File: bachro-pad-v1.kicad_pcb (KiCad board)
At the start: 2 copper layers, 12 x 20.6 mm, 39 parts, among them J0 OLED_128x32, SW1 RotaryEncoder_Switch, SW10 RotaryEncoder_Switch, SW11 RotaryEncoder_Switch, SW12 RotaryEncoder_Switch, SW13 RotaryEncoder_Switch, SW14 RotaryEncoder_Switch, SW15 RotaryEncoder_Switch, SW16 RotaryEncoder_Switch, SW2 RotaryEncoder_Switch, SW3 RotaryEncoder_Switch, SW4 RotaryEncoder_Switch, SW5 RotaryEncoder_Switch, SW6 RotaryEncoder_Switch, SW7 RotaryEncoder_Switch, SW8 RotaryEncoder_Switch, SW9 RotaryEncoder_Switch, U1 rp2040-zero, U2 MCP23017x-x-SP, U3 MCP23017x-x-SP, U4 TRRS

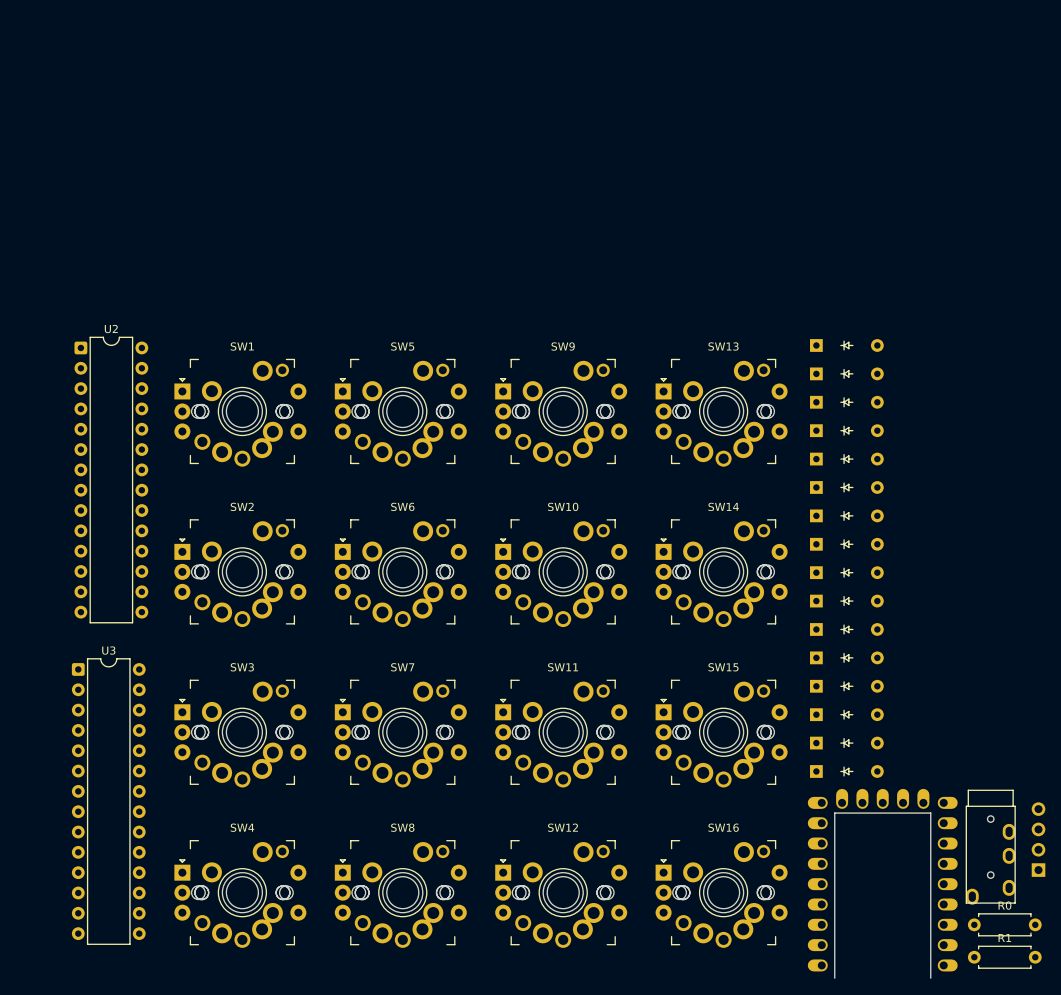
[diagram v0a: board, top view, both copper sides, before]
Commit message: Sync PCB with schematic: add decoupling caps and INT pull-up footprints
Update PCB from Schematic after adding C0/C1 (MCP23017 decoupling) and
R3-R6 (INTA/INTB pull-ups) in the schematic.
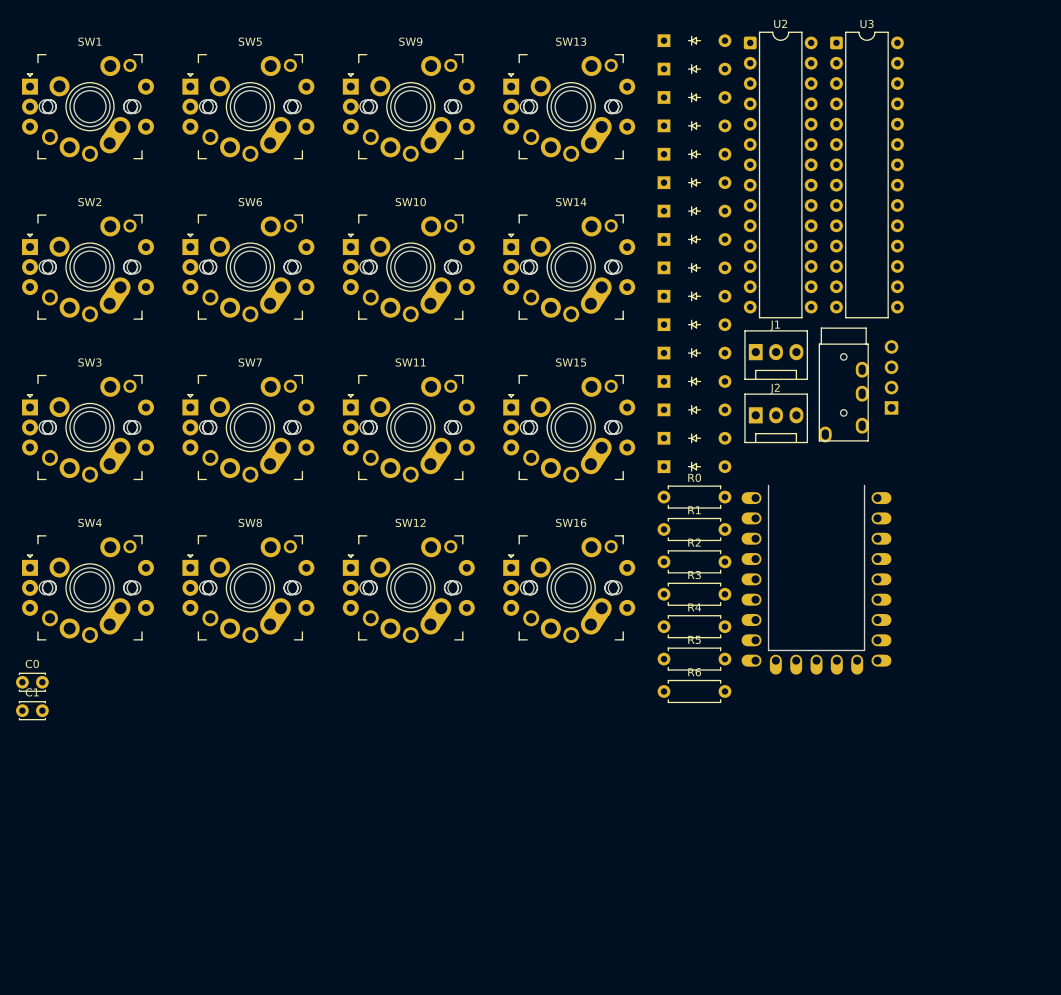
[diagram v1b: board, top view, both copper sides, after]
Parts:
- added C0: 100nF, Capacitor_THT:C_Disc_D3.0mm_W2.0mm_P2.50mm, F.Cu at (305.9, 81.5)
- added C1: 100nF, Capacitor_THT:C_Disc_D3.0mm_W2.0mm_P2.50mm, F.Cu at (305.9, 85.0)
- added J1: Conn_01x03, Connector:FanPinHeader_1x03_P2.54mm_Vertical, F.Cu at (397.5, 40.2)
- added J2: Conn_01x03, Connector:FanPinHeader_1x03_P2.54mm_Vertical, F.Cu at (397.5, 48.1)
- added R2: 10k, Resistor_THT:R_Axial_DIN0207_L6.3mm_D2.5mm_P7.62mm_Horizontal, F.Cu at (386.1, 66.4)
- added R3: 10k, Resistor_THT:R_Axial_DIN0207_L6.3mm_D2.5mm_P7.62mm_Horizontal, F.Cu at (386.1, 70.5)
- added R4: 10k, Resistor_THT:R_Axial_DIN0207_L6.3mm_D2.5mm_P7.62mm_Horizontal, F.Cu at (386.1, 74.5)
- added R5: 10k, Resistor_THT:R_Axial_DIN0207_L6.3mm_D2.5mm_P7.62mm_Horizontal, F.Cu at (386.1, 78.6)
- added R6: 10k, Resistor_THT:R_Axial_DIN0207_L6.3mm_D2.5mm_P7.62mm_Horizontal, F.Cu at (386.1, 82.6)
- R0, R1: value Resistor -> 4.7k
- moved U3 122.9 mm to (407.6, 1.55)
- moved U2 91.9 mm to (396.9, 1.55)
- moved R0 66.1 mm to (386.1, 58.3)
- moved R1 66.1 mm to (386.1, 62.4)
- moved J0 60.6 mm to (412.9, 37.4)
- moved U4 60.6 mm to (408.5, 39.2)
- moved D1 42.6 mm to (386.1, 1.27)
- moved D10 42.6 mm to (386.1, 33.2)
- moved D11 42.6 mm to (386.1, 36.8)
- moved D14 42.6 mm to (386.1, 47.4)
- moved D15 42.6 mm to (386.1, 51.0)
- moved D16 42.6 mm to (386.1, 54.5)
- moved D3 42.6 mm to (386.1, 8.38)
- moved D5 42.6 mm to (386.1, 15.5)
- moved D6 42.6 mm to (386.1, 19.0)
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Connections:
- J0 pad 2: 3V3 -> +3V3
- U1 pad 17: unconnected-(U1-26-Pad17) -> DEBUG_TX
- U1 pad 18: unconnected-(U1-27-Pad18) -> DEBUG_RX
- U1 pad 19: unconnected-(U1-28-Pad19) -> TETHER_DETECT
- U1 pad 20: unconnected-(U1-29-Pad20) -> SPARE_ADC
- U1 pad 21: 3V3 -> +3V3
- U2 pad 18: 3V3 -> +3V3
- U2 pad 9: 3V3 -> +3V3
- U3 pad 15: 3V3 -> +3V3
- U3 pad 18: 3V3 -> +3V3
- U3 pad 9: 3V3 -> +3V3
- U4 pad 3: 3V3 -> TETHER_DETECT

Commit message: First draft
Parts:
- J1, J2, U1: moved to B.Cu
- moved U3 303.5 mm to (121.3, 102.2), turned to 180 degrees
- moved U1 285.7 mm to (124.0, 17.8), turned to -90 degrees
- moved U2 282.3 mm to (121.4, 63.3), turned to 180 degrees
- moved R0 267.3 mm to (124.0, 6.10)
- moved J0 262.4 mm to (150.8, 24.4), turned to 180 degrees
- moved R1 258.2 mm to (134.1, 6.10)
- moved SW13 255.9 mm to (133.3, 95.2)
- moved R2 242.0 mm to (151.8, 6.10), turned to 180 degrees
- moved R6 236.9 mm to (161.9, 6.10), turned to 180 degrees
- moved SW14 231.6 mm to (152.4, 95.2)
- moved J1 231.2 mm to (168.3, 10.2), turned to -90 degrees
- moved SW9 230.9 mm to (133.3, 76.2)
- moved D1 229.9 mm to (156.8, 19.1), turned to -90 degrees
- moved D5 226.7 mm to (159.4, 19.1), turned to -90 degrees
- moved R5 225.9 mm to (172.1, 6.10), turned to 180 degrees
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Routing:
- net gnd: track 0.00 -> 522.2 mm, vias 0 -> 3
- net +3V3: track 0.00 -> 223.4 mm, vias 0 -> 3
- net col 4: track 0.00 -> 197.1 mm
- net col 3: track 0.00 -> 189.1 mm
- net col 2: track 0.00 -> 184.3 mm
- net col 1: track 0.00 -> 147.9 mm, vias 0 -> 1
- net SDA: track 0.00 -> 124.5 mm, vias 0 -> 1
- net U3 INTA: track 0.00 -> 124.5 mm, vias 0 -> 2
- net SCL: track 0.00 -> 114.6 mm, vias 0 -> 1
- net U3 INTB: track 0.00 -> 111.9 mm, vias 0 -> 2
- net U2 INTA: track 0.00 -> 110.0 mm, vias 0 -> 2
- net Net-(D13-A): track 0.00 -> 106.8 mm
- net Net-(D14-A): track 0.00 -> 98.5 mm
- net row 1: track 0.00 -> 94.9 mm, vias 0 -> 3
- net U2 INTB: track 0.00 -> 93.3 mm, vias 0 -> 2
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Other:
- board size 12 x 20.6 mm -> 89.5 x 103.5 mm
- board text added: "+3v3"
- board text added: "BACHROPAD"
- board text added: "GND"
- board text added: "GP29"
- board text added: "RX"
- board text added: "TX"
- board text added: "by joni"

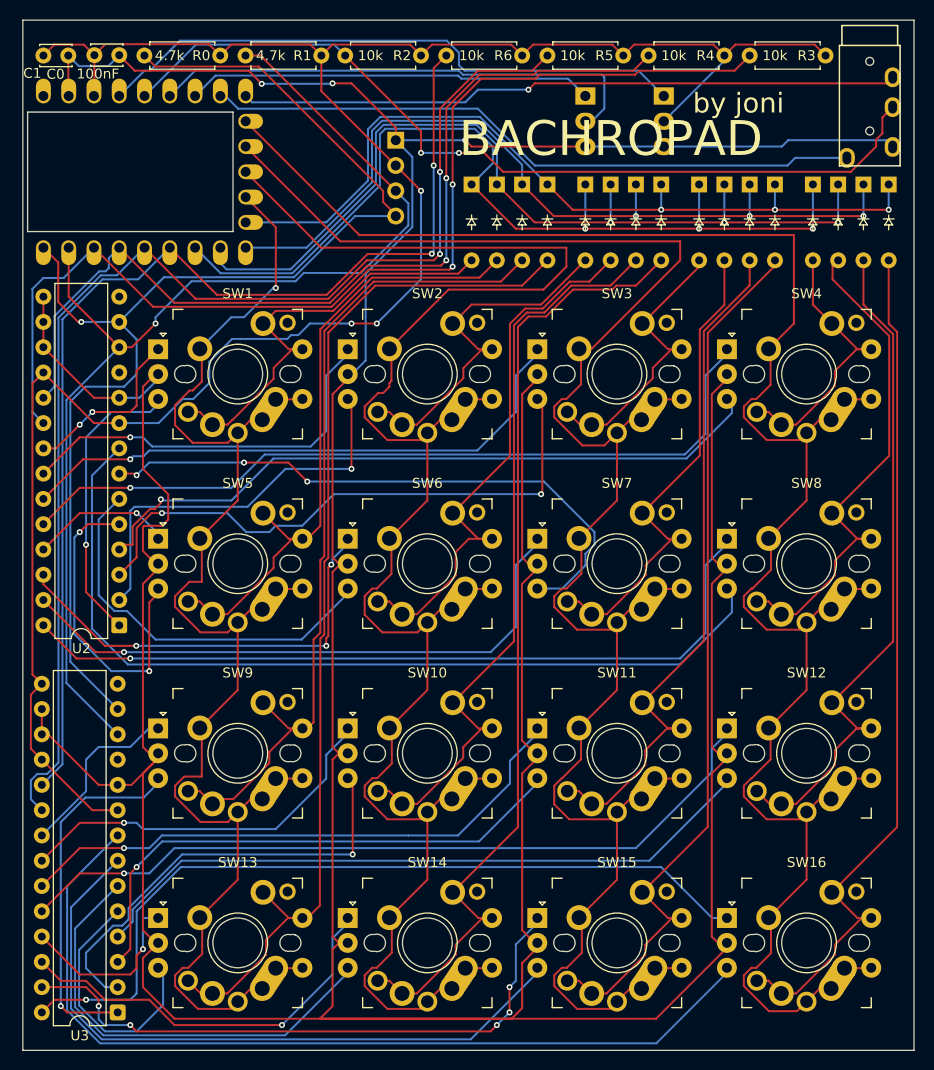
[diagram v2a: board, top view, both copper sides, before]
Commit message: updating layout to fix silk screen warnings
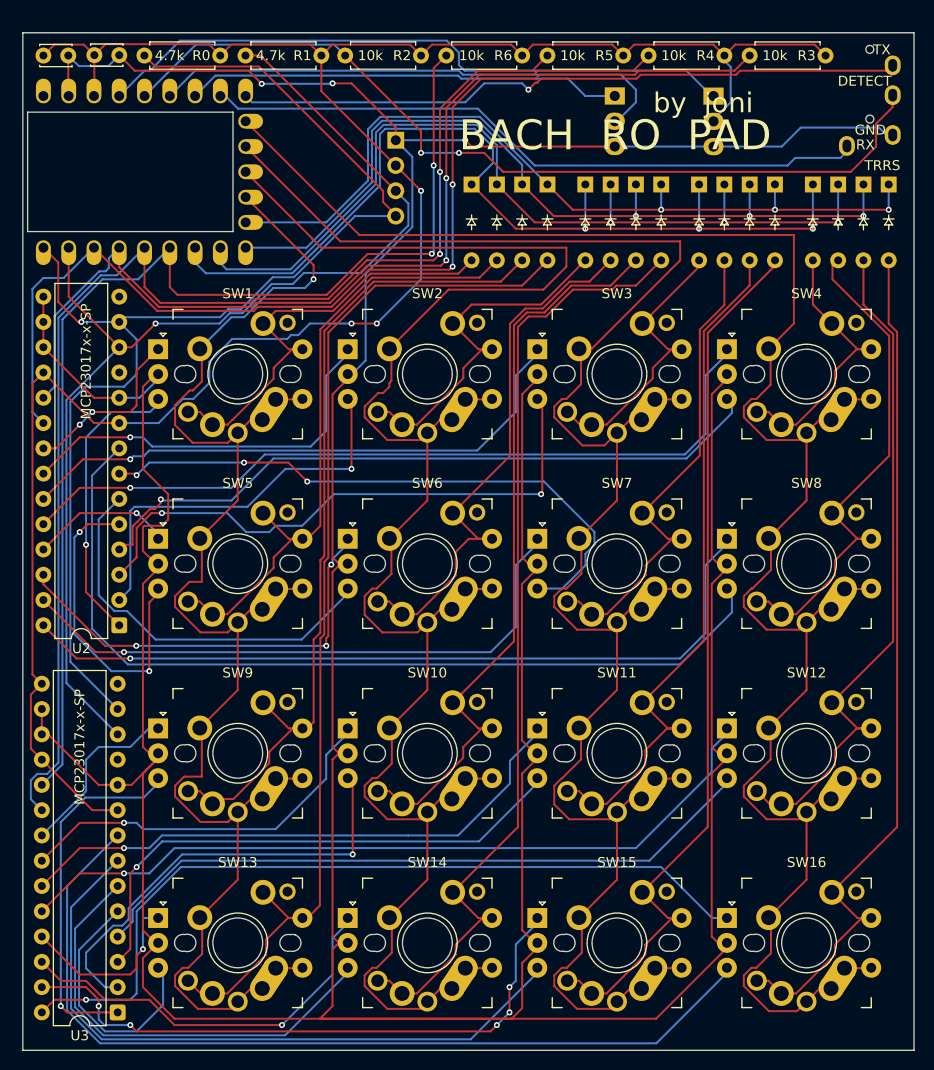
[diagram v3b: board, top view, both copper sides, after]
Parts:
- moved J2 5.00 mm to (181.2, 10.2)
- moved J1 2.96 mm to (171.2, 10.2)
- moved U4 1.20 mm to (196.9, 3.88)
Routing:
- net col 1: track 147.9 -> 152.8 mm
- net SPARE_ADC: track 60.0 -> 64.9 mm
- net DEBUG_RX: track 50.6 -> 53.3 mm
- net U3 INTA: track 124.5 -> 127.2 mm
- net DEBUG_TX: track 40.9 -> 43.4 mm
- net U3 INTB: track 111.9 -> 114.2 mm
- net U2 INTB: track 93.3 -> 94.8 mm
- net +3V3: track 223.4 -> 221.9 mm
- net SPLIT_TX: track 66.3 -> 67.4 mm
- net row 1: track 94.9 -> 95.8 mm
- net SPLIT_RX: track 66.2 -> 67.0 mm
- net gnd: track 522.2 -> 522.9 mm
- net TETHER_DETECT: track 87.9 -> 88.5 mm
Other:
- board size 89.5 x 103.5 mm -> 89.5 x 102.2 mm
- board text added: "BACH RO PAD"
- board text removed: "BACHROPAD"

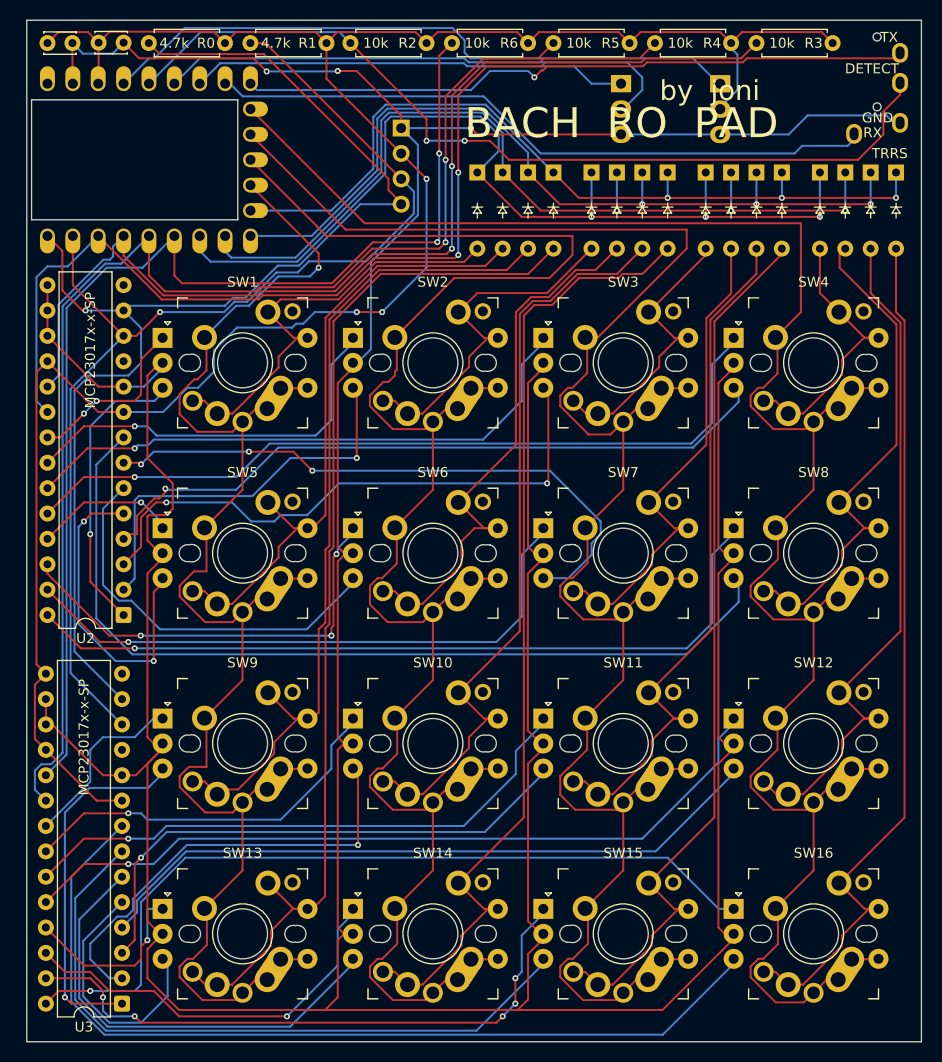
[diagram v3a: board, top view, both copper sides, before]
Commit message: resizing brd
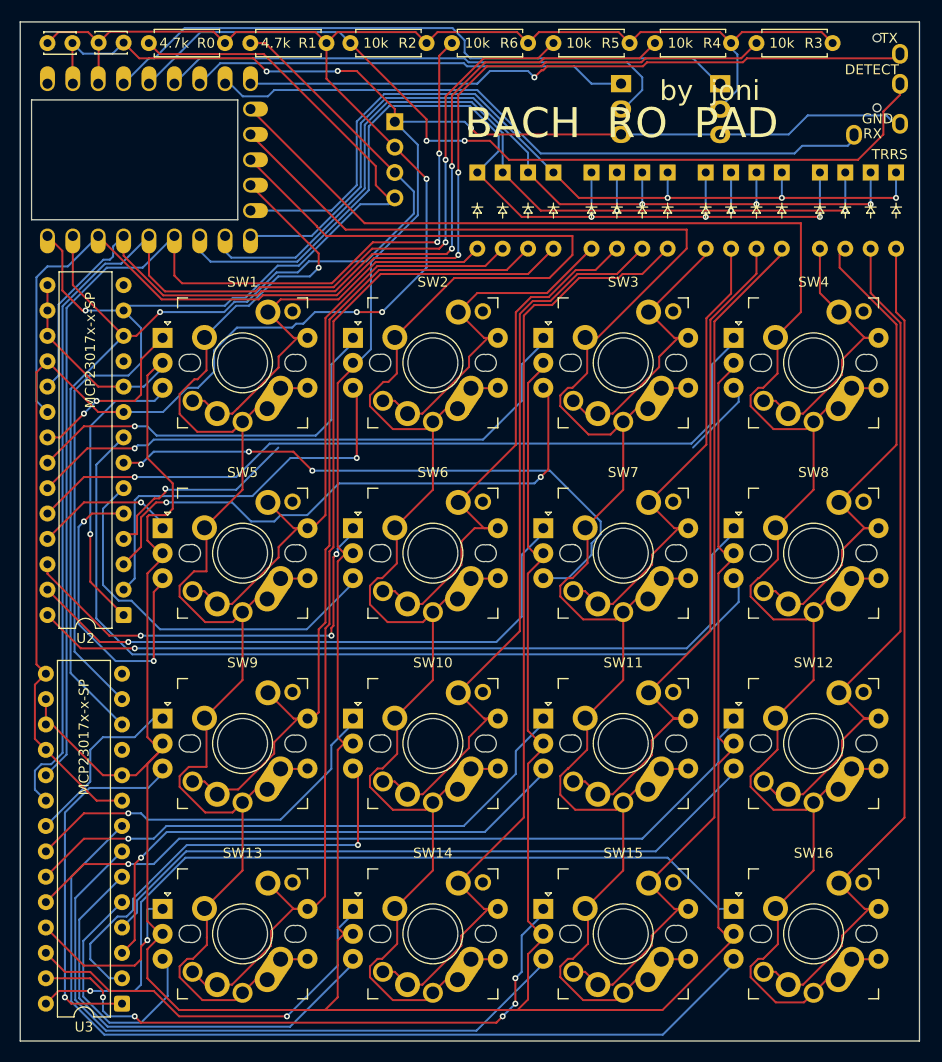
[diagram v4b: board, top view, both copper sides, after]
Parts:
- moved J0 0.90 mm to (150.2, 23.8)
- moved U4 0.10 mm to (196.8, 3.98)
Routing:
- net B SW4: track 70.0 -> 28.5 mm
- net row 2: track 90.7 -> 92.3 mm
- net row 4: track 83.5 -> 85.1 mm
- net row 3: track 85.0 -> 86.6 mm
- net row 1: track 95.8 -> 97.4 mm
- net SPLIT_RX: track 67.0 -> 67.9 mm
- net TETHER_DETECT: track 88.5 -> 89.3 mm
- net B SW3: track 58.7 -> 57.9 mm
- net SDA: track 124.5 -> 123.8 mm
- net gnd: track 522.9 -> 523.6 mm
- net SCL: track 114.2 -> 114.8 mm
- net SPLIT_TX: track 67.4 -> 66.8 mm
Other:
- board size 89.5 x 102.2 mm -> 90 x 102 mm
